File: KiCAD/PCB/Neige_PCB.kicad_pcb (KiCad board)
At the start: 2 copper layers, 257 x 57.1 mm, 93 parts, among them J1 TYPE-C 16PIN 2MD(073), SW1 SW_Push, SW10 SW_Push, SW11 SW_Push, SW12 SW_Push, SW13 SW_Push, SW14 SW_Push, SW15 SW_Push, SW16 SW_Push, SW17 SW_Push, SW18 SW_Push, SW19 SW_Push, SW2 SW_Push, SW20 SW_Push, SW21 SW_Push, SW22 SW_Push, SW23 SW_Push, SW24 SW_Push, SW25 SW_Push, SW26 SW_Push, SW27 SW_Push, SW28 SW_Push, SW29 SW_Push, SW3 SW_Push, SW30 SW_Push, SW31 SW_Push, SW32 SW_Push, SW33 SW_Push, SW34 SW_Push, SW35 SW_Push, SW36 SW_Push, SW4 SW_Push, SW5 SW_Push, SW6 SW_Push, SW7 SW_Push, SW8 SW_Push, SW9 SW_Push, U1 USBLC6-2SC6, U2 XC6206P332MR, U3 STM32F072CBU6

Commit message: v1.0
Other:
- board text removed: "JLCJLCJLCJLC"
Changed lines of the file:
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@@
 		(layer "Edge.Cuts")
-	)
-	(gr_text "JLCJLCJLCJLC"
-		(at 93.3498 76.4248 90)
-		(layer "B.SilkS")
-		(effects
-			(font
-				(size 1 1)
-				(thickness 0.15)
-			)
-			(justify left bottom mirror)
-		)
 	)
 	(gr_text "Neige PCB v1.0 by @ymkn"

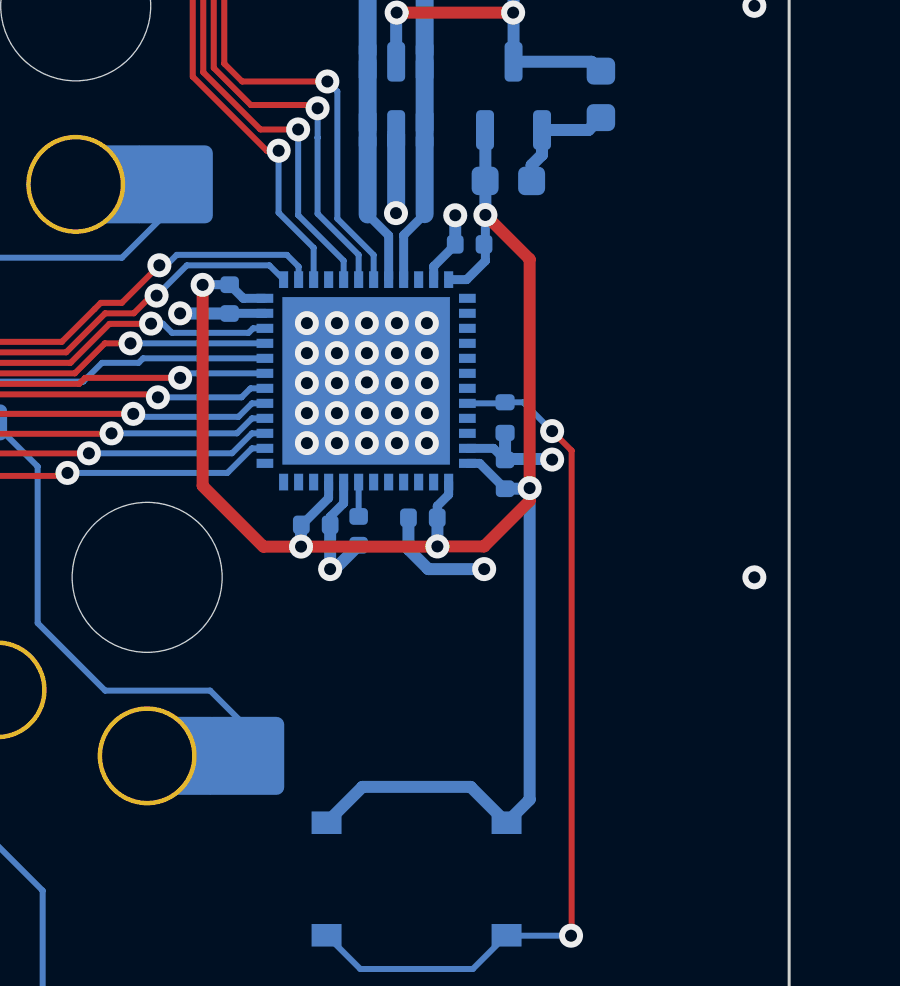
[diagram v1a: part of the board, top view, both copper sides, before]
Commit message: パスコン見直し版
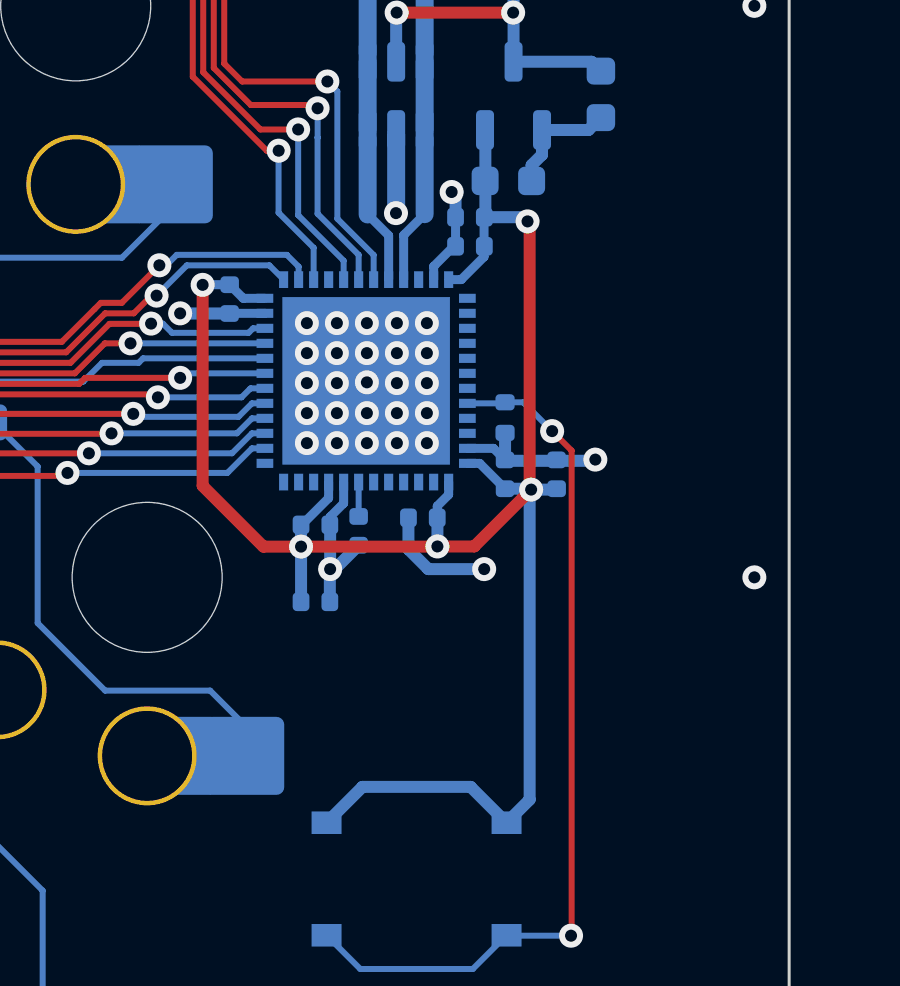
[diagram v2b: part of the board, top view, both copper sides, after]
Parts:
- added C11: 4.7uF, Capacitor_SMD:C_0402_1005Metric, B.Cu at (337.5, 72.8)
- added C12: 4.7uF, Capacitor_SMD:C_0402_1005Metric, B.Cu at (334.6, 64.2)
- added C13: 1uF, Capacitor_SMD:C_0402_1005Metric, B.Cu at (329.5, 77.0)
- C9: value 100nF -> 10nF
- moved C6 0.07 mm to (334.6, 65.2)
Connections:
- U3 pad 5: XIN -> unconnected-(U3-PF0-Pad5)
- U3 pad 6: XOUT -> unconnected-(U3-PF1-Pad6)
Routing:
- net GND: track 30.7 -> 34.1 mm
- net +3V3: track 62.7 -> 65.8 mm
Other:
- board text added: "neige PCB v1.1 by @ymkn"
- board text removed: "Neige PCB v1.0 by @ymkn"
